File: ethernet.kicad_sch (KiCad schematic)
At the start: 32 parts, among them J1 HR911105A, U35 LAN8742A, Y1 25MHz

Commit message: Finished annotation
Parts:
- renumbered C17 to C501, C75 to C502, C77 to C503, C79 to C504, C81 to C505, C83 to C506, C87 to C507, C89 to C508, C91 to C509, C93 to C510, J1 to J501, L5 to L501, R23 to R501, R24 to R502, R25 to R503, R26 to R504, R27 to R505, R28 to R506, R29 to R507, R30 to R508, R31 to R509, R32 to R510, R34 to R511, R130 to R512, R185 to R513, R187 to R514, R188 to R515, R189 to R516, R191 to R517, R195 to R518, U35 to U501, Y1 to Y501

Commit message: Fixed ERC errors and warnings
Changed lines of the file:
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@@
   (junction (at 156.21 133.35) (diameter 0) (color 0 0 0 0)
   )
+  (junction (at 193.04 57.15) (diameter 0) (color 0 0 0 0)
+  )
   (junction (at 215.9 60.96) (diameter 0) (color 0 0 0 0)
   )
@@
   (junction (at 180.34 133.35) (diameter 0) (color 0 0 0 0)
   )
+  (junction (at 193.04 60.96) (diameter 0) (color 0 0 0 0)
+  )
+  (junction (at 187.96 110.49) (diameter 0) (color 0 0 0 0)
+  )
+  (junction (at 134.62 54.61) (diameter 0) (color 0 0 0 0)
+  )
+  (junction (at 85.09 92.71) (diameter 0) (color 0 0 0 0)
+  )
   (junction (at 233.68 113.03) (diameter 0) (color 0 0 0 0)
   )
-  (junction (at 193.04 60.96) (diameter 0) (color 0 0 0 0)
-  )
-  (junction (at 187.96 110.49) (diameter 0) (color 0 0 0 0)
-  )
-  (junction (at 134.62 54.61) (diameter 0) (color 0 0 0 0)
-  )
-  (junction (at 85.09 92.71) (diameter 0) (color 0 0 0 0)
-  )
   (junction (at 96.52 113.03) (diameter 0) (color 0 0 0 0)
   )
@@
   (junction (at 204.47 60.96) (diameter 0) (color 0 0 0 0)
   )
+  (junction (at 147.32 57.15) (diameter 0) (color 0 0 0 0)
+  )
   (junction (at 81.28 102.87) (diameter 0) (color 0 0 0 0)
   )
@@
     (stroke (width 0) (type default))
   )
-  (wire (pts (xy 228.6 102.87) (xy 228.6 113.03))
-    (stroke (width 0) (type default))
-  )
-  (wire (pts (xy 193.04 55.88) (xy 193.04 60.96))
+  (wire (pts (xy 193.04 55.88) (xy 193.04 57.15))
     (stroke (width 0) (type default))
   )
@@
     (stroke (width 0) (type default))
   )
+  (wire (pts (xy 233.68 113.03) (xy 233.68 121.92))
+    (stroke (width 0) (type default))
+  )
   (wire (pts (xy 58.42 110.49) (xy 129.54 110.49))
     (stroke (width 0) (type default))
@@
     (stroke (width 0) (type default))
   )
+  (wire (pts (xy 233.68 113.03) (xy 228.6 113.03))
+    (stroke (width 0) (type default))
+  )
   (wire (pts (xy 170.18 87.63) (xy 167.64 87.63))
     (stroke (width 0) (type default))
@@
     (stroke (width 0) (type default))
   )
-  (wire (pts (xy 228.6 113.03) (xy 233.68 113.03))
-    (stroke (width 0) (type default))
-  )
   (wire (pts (xy 85.09 52.07) (xy 85.09 58.42))
     (stroke (width 0) (type default))
   )
+  (wire (pts (xy 228.6 113.03) (xy 228.6 102.87))
+    (stroke (width 0) (type default))
+  )
   (wire (pts (xy 134.62 66.04) (xy 134.62 69.85))
     (stroke (width 0) (type default))
@@
     (stroke (width 0) (type default))
   )
+  (wire (pts (xy 147.32 57.15) (xy 147.32 54.61))
+    (stroke (width 0) (type default))
+  )
   (wire (pts (xy 251.46 97.79) (xy 251.46 101.6))
     (stroke (width 0) (type default))
@@
     (stroke (width 0) (type default))
   )
-  (wire (pts (xy 233.68 113.03) (xy 233.68 121.92))
-    (stroke (width 0) (type default))
-  )
   (wire (pts (xy 170.18 80.01) (xy 170.18 87.63))
     (stroke (width 0) (type default))
@@
     (stroke (width 0) (type default))
   )
-  (wire (pts (xy 147.32 69.85) (xy 147.32 54.61))
+  (wire (pts (xy 147.32 69.85) (xy 147.32 57.15))
     (stroke (width 0) (type default))
   )
@@
   )
   (wire (pts (xy 96.52 66.04) (xy 96.52 113.03))
+    (stroke (width 0) (type default))
+  )
+  (wire (pts (xy 193.04 57.15) (xy 193.04 60.96))
     (stroke (width 0) (type default))
   )
@@
         (path "/894df1c3-1a5d-48b0-9966-84d5c2c2c705/0815129a-f835-434b-a91c-b449ee32428d/ea9984c4-789d-45e6-9ac4-f6ee67efc41e"
           (reference "C906") (unit 1)
+        )
+      )
+    )
+  )
+  (symbol (lib_id "power:PWR_FLAG") (at 147.32 57.15 270) (unit 1)
+    (in_bom yes) (on_board yes) (dnp no) (fields_autoplaced)
+    (property "Reference" "#FLG0501" (at 149.225 57.15 0)
+      (effects (font (size 1.27 1.27)) hide)
+    )
+    (property "Value" "PWR_FLAG" (at 151.13 57.15 90)
+      (effects (font (size 1.27 1.27)) (justify left))
+    )
+    (property "Footprint" "" (at 147.32 57.15 0)
+      (effects (font (size 1.27 1.27)) hide)
+    )
+    (property "Datasheet" "~" (at 147.32 57.15 0)
+      (effects (font (size 1.27 1.27)) hide)
+    )
+    (pin "1")
+    (instances
+      (project "cad-enc-dec"
+        (path "/894df1c3-1a5d-48b0-9966-84d5c2c2c705/7b82f1b8-f670-4c54-86aa-68b09b673554/f0d5083a-a3e1-4f4f-9a6a-0e69c3027d6d"
+          (reference "#FLG0501") (unit 1)
+        )
+        (path "/894df1c3-1a5d-48b0-9966-84d5c2c2c705/0815129a-f835-434b-a91c-b449ee32428d/ea9984c4-789d-45e6-9ac4-f6ee67efc41e"
+          (reference "#FLG0901") (unit 1)
         )
       )
@@
         )
       )
+    )
+  )
+  (symbol (lib_id "power:PWR_FLAG") (at 193.04 57.15 270) (unit 1)
+    (in_bom yes) (on_board yes) (dnp no) (fields_autoplaced)
+    (property "Reference" "#FLG0502" (at 194.945 57.15 0)
+      (effects (font (size 1.27 1.27)) hide)
+    )
+    (property "Value" "PWR_FLAG" (at 196.85 57.15 90)
+      (effects (font (size 1.27 1.27)) (justify left))
+    )
+    (property "Footprint" "" (at 193.04 57.15 0)
+      (effects (font (size 1.27 1.27)) hide)
+    )
+    (property "Datasheet" "~" (at 193.04 57.15 0)
+      (effects (font (size 1.27 1.27)) hide)
+    )
+    (pin "1")
+    (instances
+      (project "cad-enc-dec"
+        (path "/894df1c3-1a5d-48b0-9966-84d5c2c2c705/7b82f1b8-f670-4c54-86aa-68b09b673554/f0d5083a-a3e1-4f4f-9a6a-0e69c3027d6d"
+          (reference "#FLG0502") (unit 1)
+        )
+        (path "/894df1c3-1a5d-48b0-9966-84d5c2c2c705/0815129a-f835-434b-a91c-b449ee32428d/ea9984c4-789d-45e6-9ac4-f6ee67efc41e"
+          (reference "#FLG0902") (unit 1)
+        )
+      )

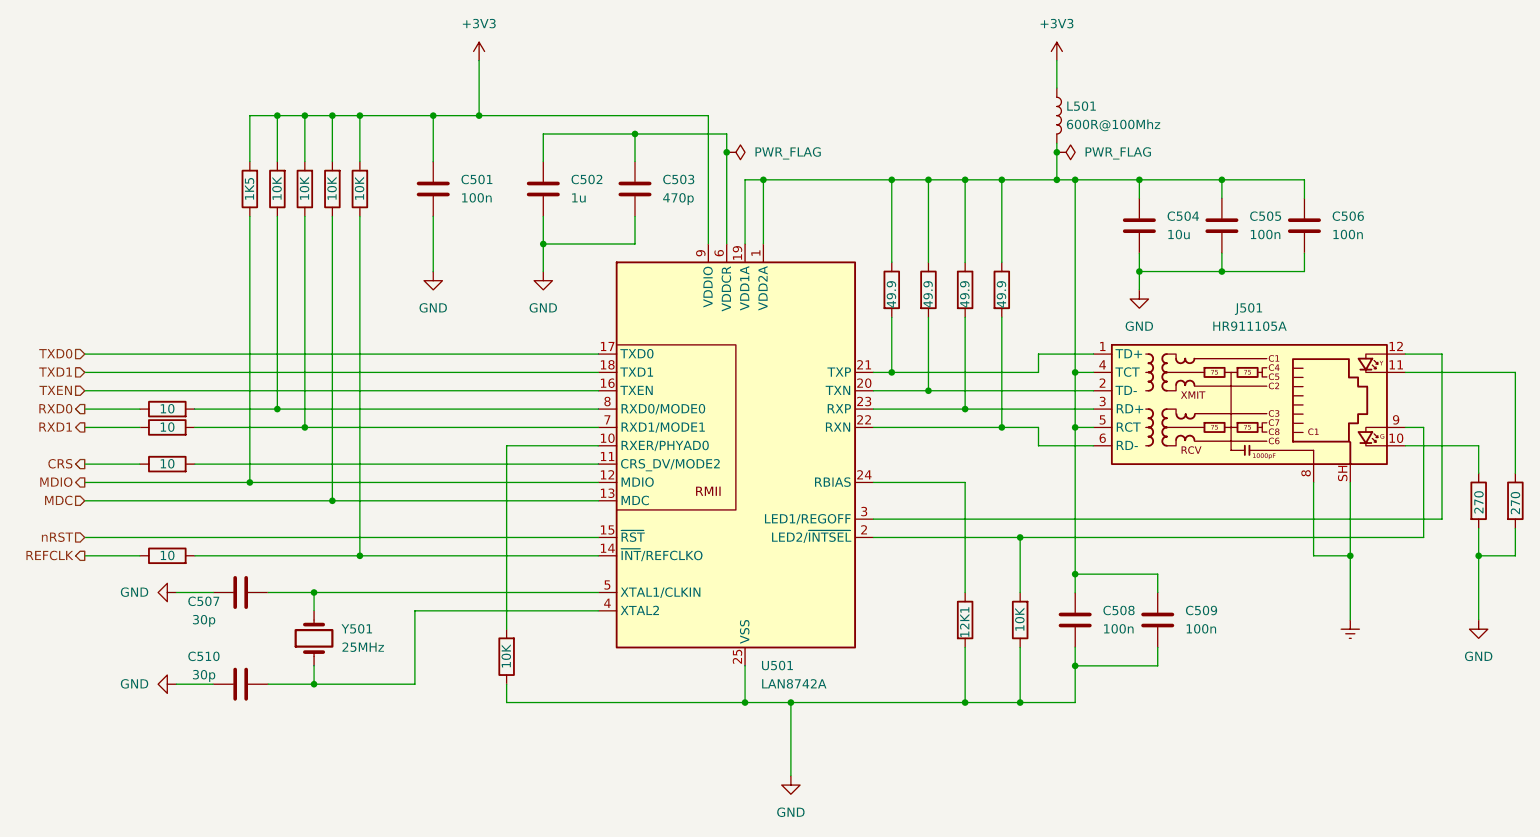
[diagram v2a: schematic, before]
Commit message: Split schematic into three subprojects
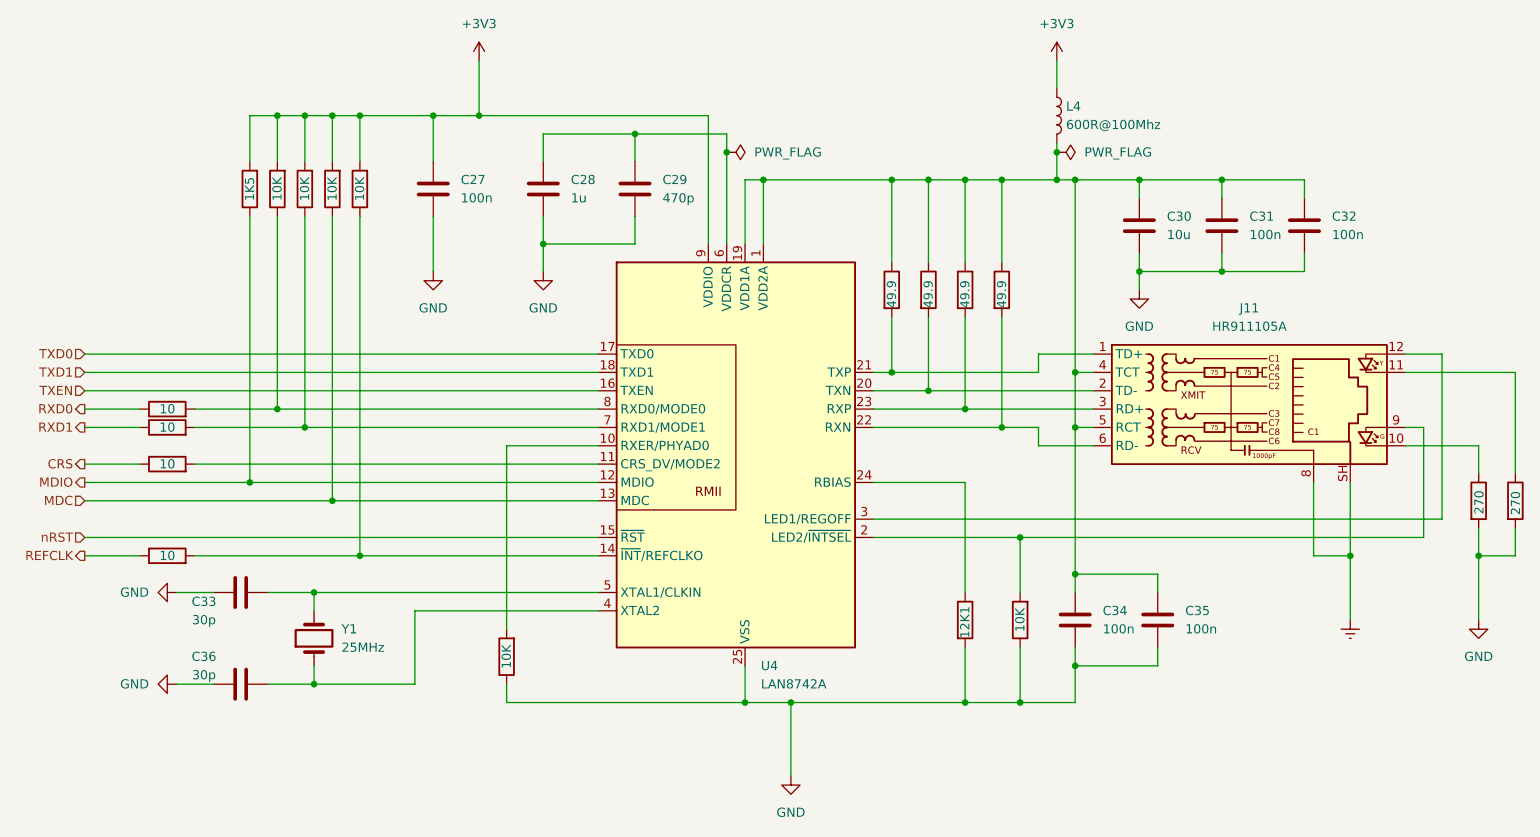
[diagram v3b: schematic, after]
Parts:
- renumbered C501 to C27, C502 to C28, C503 to C29, C504 to C30, C505 to C31, C506 to C32, C507 to C33, C508 to C34, C509 to C35, C510 to C36, J501 to J11, L501 to L4, R503 to R10, R504 to R11, R505 to R12, R506 to R13, R507 to R14, R508 to R15, R509 to R16, R510 to R17, R511 to R18, R512 to R19, R513 to R20, R514 to R21, R515 to R22, R516 to R23, R517 to R24, R518 to R25, R501 to R8, R502 to R9, U501 to U4, Y501 to Y1

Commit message: Updated designators positions
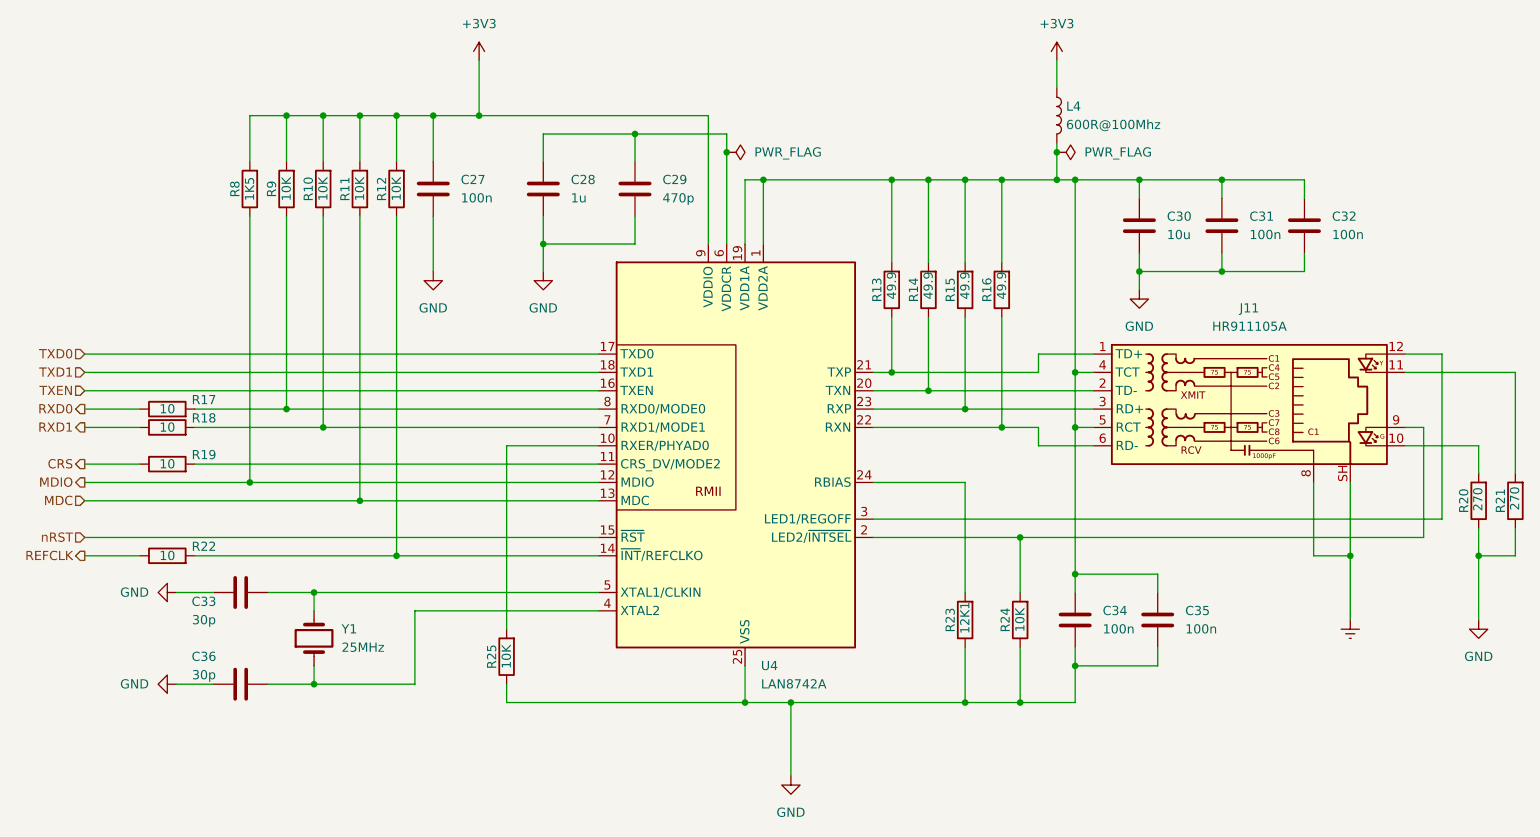
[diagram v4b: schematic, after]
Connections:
- net GND: now also R20.1, R21.1, R23.1; no longer R20.2, R21.2, R23.2
- net at J11.10: now also R20.2; no longer R20.1
- net at C30.1, C31.1, C32.1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: now also R13.2, R14.2, R15.2, R16.2; no longer R13.1, R14.1, R15.1, R16.1
- net at J11.2 (TD-), U4.20 (TXN): now also R14.1; no longer R14.2
- net at J11.1 (TD+), U4.21 (TXP): now also R13.1; no longer R13.2
- net at J11.6 (RD-), U4.22 (RXN): now also R16.1; no longer R16.2
- net at J11.3 (RD+), U4.23 (RXP): now also R15.1; no longer R15.2
- net at U4.24 (RBIAS): now also R23.2; no longer R23.1
- net at J11.11: now also R21.2; no longer R21.1

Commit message: Set capacitor and resistor values on tranciever circuits
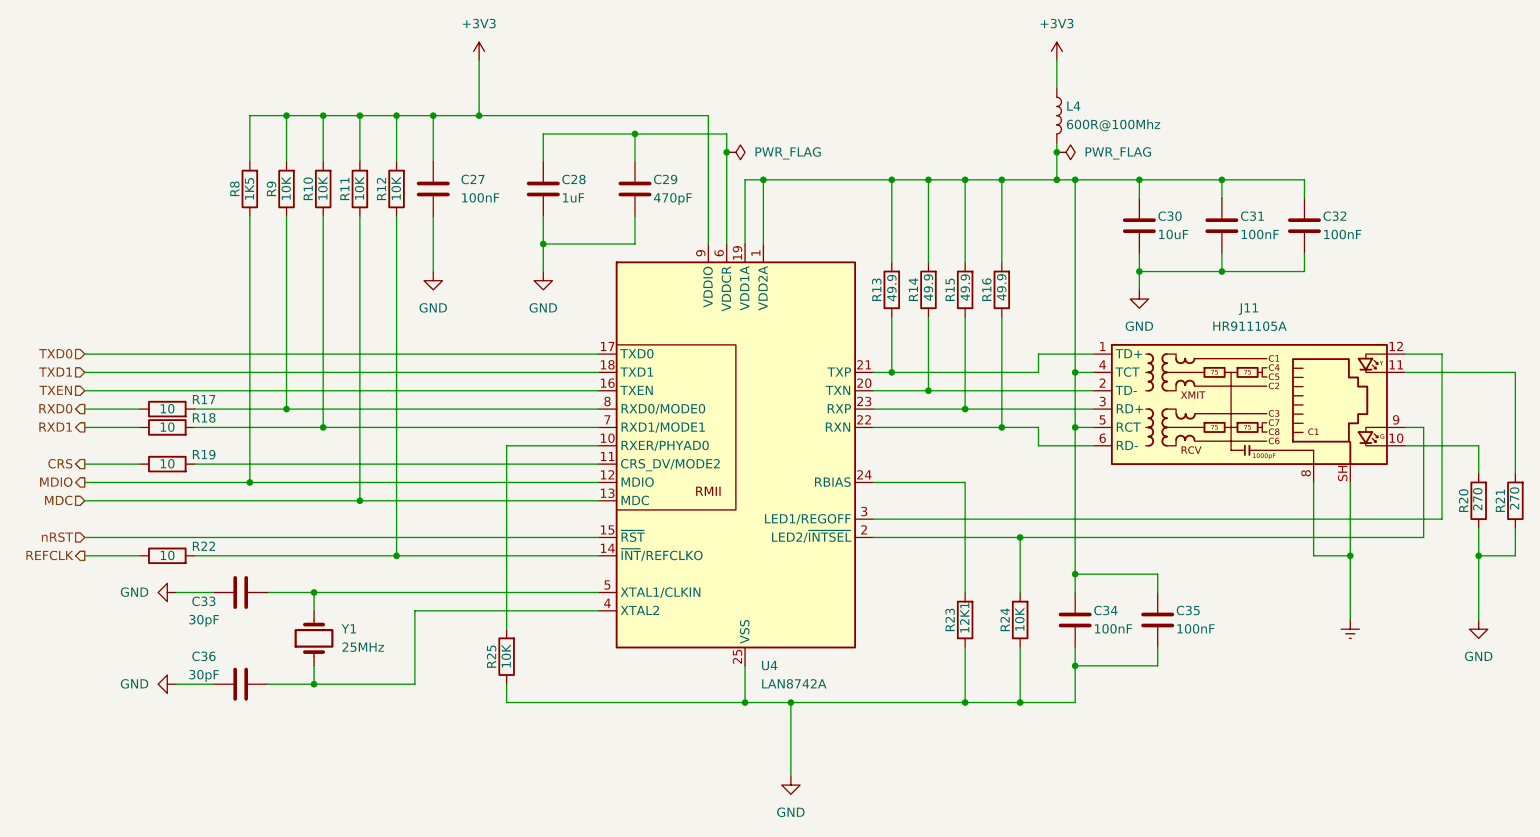
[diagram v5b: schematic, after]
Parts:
- C27, C31, C32, C34, C35: value 100n -> 100nF
- C28: value 1u -> 1uF
- C29: value 470p -> 470pF
- C30: value 10u -> 10uF
- C33, C36: value 30p -> 30pF

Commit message: Assigned footprints for digital components
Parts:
- removed Y1: 25MHz, Crystal:Crystal_SMD_HC49-SD, symbol Device:Crystal
- added Y1: ABM8G-25MHz, Crystal:Crystal_SMD_3225-4Pin_3.2x2.5mm_HandSoldering, symbol Device:Crystal_GND24
- U4: value LAN8742A -> LAN8742AI
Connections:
- net GND: now also Y1.2, Y1.4
- net at C33.2, U4.5 (XTAL1/CLKIN): now also Y1.3
- net at C36.2, U4.4 (XTAL2): now also Y1.1
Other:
- moved on the sheet: C33, C36

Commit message: Redone power input circuit
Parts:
- renumbered C27 to C29, C28 to C30, C29 to C31, C30 to C32, C31 to C33, C32 to C34, C33 to C35, C34 to C36, C35 to C37, C36 to C38, R11 to R10, R12 to R11, R13 to R12, R14 to R13, R15 to R14, R16 to R15, R17 to R16, R18 to R17, R19 to R18, R20 to R19, R21 to R20, R22 to R21, R23 to R22, R24 to R23, R25 to R24, R8 to R7, R9 to R8, R10 to R9, U4 to U5

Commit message: Optimized components by cost and footprint size
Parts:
- renumbered C35 to C27, C38 to C28, C36 to C32, C32 to C33, C37 to C34, C33 to C35, C34 to C36, J11 to J10, R21 to R10, R7 to R11, R8 to R12, R9 to R13, R10 to R14, R11 to R15, R24 to R16, R12 to R17, R13 to R18, R14 to R19, R22 to R20, R15 to R21, R23 to R22, R19 to R23, R20 to R24, R16 to R7, R17 to R8, R18 to R9, U5 to U4
